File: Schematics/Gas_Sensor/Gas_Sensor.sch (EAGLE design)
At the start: 7 parts, among them J1 RJ45

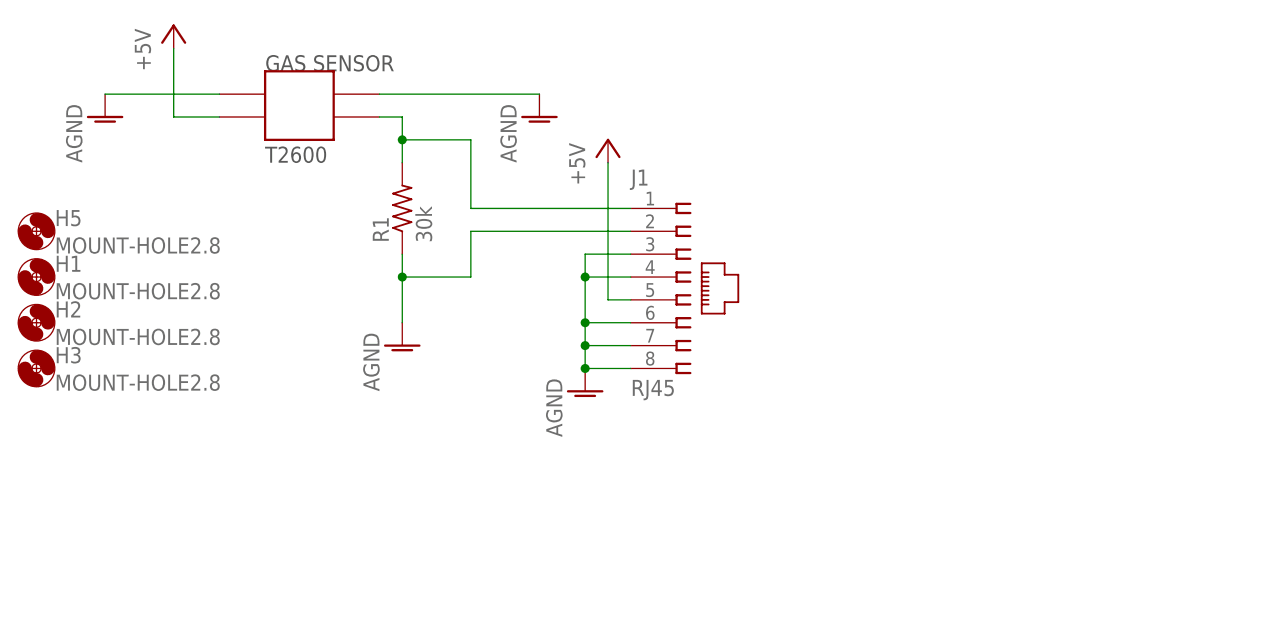
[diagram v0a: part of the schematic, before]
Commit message: Updated Sensor Module PCBs
Switched Ethernet I/O. Rerouted PCB
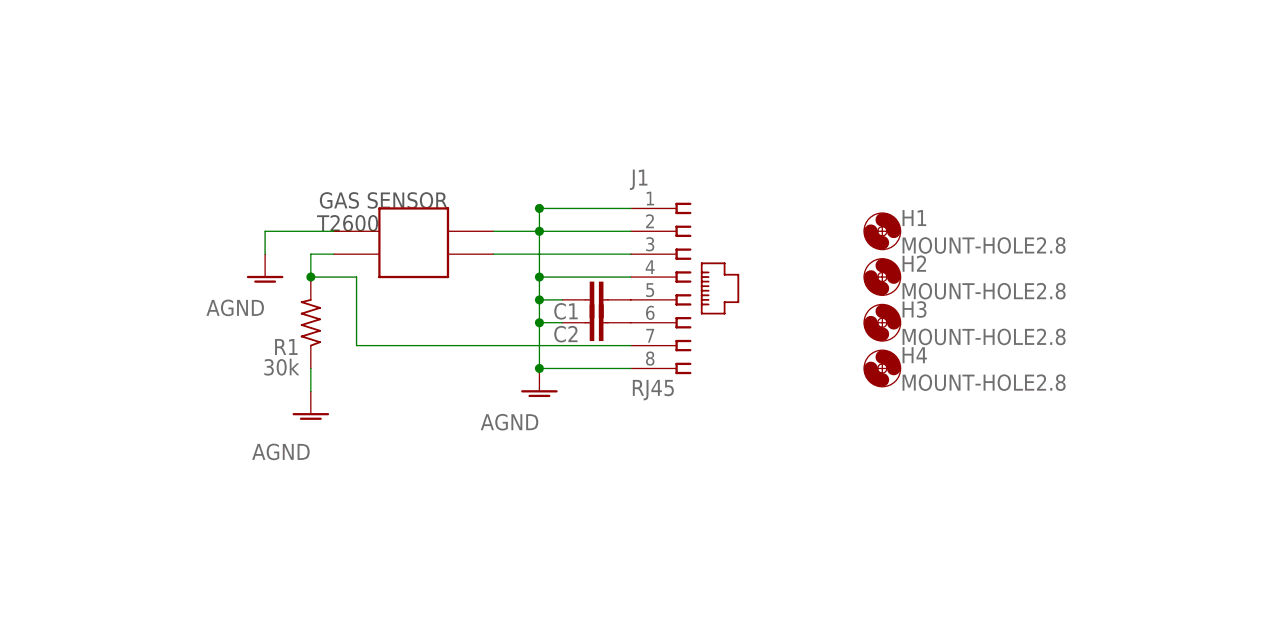
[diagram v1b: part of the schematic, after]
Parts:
- removed H5: MOUNT-HOLE2.8, holes:MOUNT-HOLE2.8
- added C1, C2: (no value), rcl:C-EUC0603K
- added H4: MOUNT-HOLE2.8, holes:MOUNT-HOLE2.8
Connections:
- removed net +5V: J1.5, U$1.P$3
- new net N$24: C2.1, J1.6
- new net N$25: C1.1, J1.5
- new net N$26: J1.3, U$1.P$3
- net AGND: now also C1.2, C2.2, J1.1; no longer J1.3, J1.6, J1.7
- net N$2: now also J1.7; no longer J1.1
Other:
- moved on the sheet: H1, H2, H3, R1

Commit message: Began PCB Verify. Slight Modifications to Gas Sensor Module during verify.
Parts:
- renumbered U$1 to X1
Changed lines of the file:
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@@
 <grid distance="0.1" unitdist="inch" unit="inch" style="lines" multiple="1" display="no" altdistance="0.01" altunitdist="inch" altunit="inch"/>
 <layers>
-<layer number="1" name="Top" color="4" fill="1" visible="no" active="no"/>
-<layer number="16" name="Bottom" color="1" fill="1" visible="no" active="no"/>
-<layer number="17" name="Pads" color="2" fill="1" visible="no" active="no"/>
-<layer number="18" name="Vias" color="2" fill="1" visible="no" active="no"/>
-<layer number="19" name="Unrouted" color="6" fill="1" visible="no" active="no"/>
-<layer number="20" name="Dimension" color="15" fill="1" visible="no" active="no"/>
-<layer number="21" name="tPlace" color="7" fill="1" visible="no" active="no"/>
-<layer number="22" name="bPlace" color="7" fill="1" visible="no" active="no"/>
-<layer number="23" name="tOrigins" color="15" fill="1" visible="no" active="no"/>
-<layer number="24" name="bOrigins" color="15" fill="1" visible="no" active="no"/>
-<layer number="25" name="tNames" color="7" fill="1" visible="no" active="no"/>
-<layer number="26" name="bNames" color="7" fill="1" visible="no" active="no"/>
-<layer number="27" name="tValues" color="7" fill="1" visible="no" active="no"/>
-<layer number="28" name="bValues" color="7" fill="1" visible="no" active="no"/>
+<layer number="1" name="Top" color="4" fill="1" visible="yes" active="no"/>
+<layer number="16" name="Bottom" color="1" fill="1" visible="yes" active="no"/>
+<layer number="17" name="Pads" color="2" fill="1" visible="yes" active="no"/>
+<layer number="18" name="Vias" color="2" fill="1" visible="yes" active="no"/>
+<layer number="19" name="Unrouted" color="6" fill="1" visible="yes" active="no"/>
+<layer number="20" name="Dimension" color="15" fill="1" visible="yes" active="no"/>
+<layer number="21" name="tPlace" color="7" fill="1" visible="yes" active="no"/>
+<layer number="22" name="bPlace" color="7" fill="1" visible="yes" active="no"/>
+<layer number="23" name="tOrigins" color="15" fill="1" visible="yes" active="no"/>
+<layer number="24" name="bOrigins" color="15" fill="1" visible="yes" active="no"/>
+<layer number="25" name="tNames" color="7" fill="1" visible="yes" active="no"/>
+<layer number="26" name="bNames" color="7" fill="1" visible="yes" active="no"/>
+<layer number="27" name="tValues" color="7" fill="1" visible="yes" active="no"/>
+<layer number="28" name="bValues" color="7" fill="1" visible="yes" active="no"/>
 <layer number="29" name="tStop" color="7" fill="3" visible="no" active="no"/>
 <layer number="30" name="bStop" color="7" fill="6" visible="no" active="no"/>
@@
 <layer number="35" name="tGlue" color="7" fill="4" visible="no" active="no"/>
 <layer number="36" name="bGlue" color="7" fill="5" visible="no" active="no"/>
-<layer number="37" name="tTest" color="7" fill="1" visible="no" active="no"/>
-<layer number="38" name="bTest" color="7" fill="1" visible="no" active="no"/>
+<layer number="37" name="tTest" color="7" fill="1" visible="yes" active="no"/>
+<layer number="38" name="bTest" color="7" fill="1" visible="yes" active="no"/>
 <layer number="39" name="tKeepout" color="4" fill="11" visible="no" active="no"/>
 <layer number="40" name="bKeepout" color="1" fill="11" visible="no" active="no"/>
@@
 <layer number="44" name="Drills" color="7" fill="1" visible="no" active="no"/>
 <layer number="45" name="Holes" color="7" fill="1" visible="no" active="no"/>
-<layer number="46" name="Milling" color="3" fill="1" visible="no" active="no"/>
-<layer number="47" name="Measures" color="7" fill="1" visible="no" active="no"/>
-<layer number="48" name="Document" color="7" fill="1" visible="no" active="no"/>
-<layer number="49" name="Reference" color="7" fill="1" visible="no" active="no"/>
-<layer number="51" name="tDocu" color="7" fill="1" visible="no" active="no"/>
-<layer number="52" name="bDocu" color="7" fill="1" visible="no" active="no"/>
+<layer number="46" name="Milling" color="3" fill="1" visible="yes" active="no"/>
+<layer number="47" name="Measures" color="7" fill="1" visible="yes" active="no"/>
+<layer number="48" name="Document" color="7" fill="1" visible="yes" active="no"/>
+<layer number="49" name="Reference" color="7" fill="1" visible="yes" active="no"/>
+<layer number="51" name="tDocu" color="7" fill="1" visible="yes" active="no"/>
+<layer number="52" name="bDocu" color="7" fill="1" visible="yes" active="no"/>
 <layer number="91" name="Nets" color="2" fill="1" visible="yes" active="yes"/>
 <layer number="92" name="Busses" color="1" fill="1" visible="yes" active="yes"/>
@@
 </classes>
 <parts>
-<part name="U$1" library="figaro" deviceset="GAS_SENSOR" device=""/>
+<part name="X1" library="figaro" deviceset="GAS_SENSOR" device=""/>
 <part name="AGND1" library="supply1" deviceset="AGND" device=""/>
 <part name="R1" library="rcl" deviceset="R-US_" device="R1206" value="30k"/>
@@
 </plain>
 <instances>
-<instance part="U$1" gate="GAS" x="71.12" y="45.72" rot="MR0"/>
+<instance part="X1" gate="GAS" x="71.12" y="45.72" rot="MR0"/>
 <instance part="AGND1" gate="VR1" x="53.34" y="43.18" smashed="yes">
 <attribute name="VALUE" x="53.34" y="40.64" size="1.778" layer="96" rot="R180"/>
@@
 <wire x1="93.98" y1="43.18" x2="83.82" y2="43.18" width="0.1524" layer="91"/>
 <junction x="83.82" y="43.18"/>
-<pinref part="U$1" gate="GAS" pin="P$4"/>
+<pinref part="X1" gate="GAS" pin="P$4"/>
 <wire x1="78.74" y1="48.26" x2="83.82" y2="48.26" width="0.1524" layer="91"/>
 <wire x1="83.82" y1="48.26" x2="83.82" y2="50.8" width="0.1524" layer="91"/>
@@
 </segment>
 <segment>
-<pinref part="U$1" gate="GAS" pin="P$1"/>
+<pinref part="X1" gate="GAS" pin="P$1"/>
 <wire x1="60.96" y1="48.26" x2="53.34" y2="48.26" width="0.1524" layer="91"/>
 <pinref part="AGND1" gate="VR1" pin="AGND"/>
@@
 <segment>
 <pinref part="R1" gate="G$1" pin="2"/>
-<pinref part="U$1" gate="GAS" pin="P$2"/>
+<pinref part="X1" gate="GAS" pin="P$2"/>
 <wire x1="58.42" y1="43.18" x2="58.42" y2="45.72" width="0.1524" layer="91"/>
 <wire x1="58.42" y1="45.72" x2="60.96" y2="45.72" width="0.1524" layer="91"/>
@@
 <pinref part="J1" gate="G$1" pin="3"/>
 <wire x1="93.98" y1="45.72" x2="78.74" y2="45.72" width="0.1524" layer="91"/>
-<pinref part="U$1" gate="GAS" pin="P$3"/>
+<pinref part="X1" gate="GAS" pin="P$3"/>
 </segment>
 </net>

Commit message: Layout for final inspection
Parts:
- C1, C2: value (none) -> 0.1uF
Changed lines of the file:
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@@
 <?xml version="1.0" encoding="utf-8"?>
 <!DOCTYPE eagle SYSTEM "eagle.dtd">
-<eagle version="6.3">
+<eagle version="6.4">
 <drawing>
 <settings>
@@
 <grid distance="0.1" unitdist="inch" unit="inch" style="lines" multiple="1" display="no" altdistance="0.01" altunitdist="inch" altunit="inch"/>
 <layers>
-<layer number="1" name="Top" color="4" fill="1" visible="yes" active="no"/>
-<layer number="16" name="Bottom" color="1" fill="1" visible="yes" active="no"/>
-<layer number="17" name="Pads" color="2" fill="1" visible="yes" active="no"/>
-<layer number="18" name="Vias" color="2" fill="1" visible="yes" active="no"/>
-<layer number="19" name="Unrouted" color="6" fill="1" visible="yes" active="no"/>
-<layer number="20" name="Dimension" color="15" fill="1" visible="yes" active="no"/>
-<layer number="21" name="tPlace" color="7" fill="1" visible="yes" active="no"/>
-<layer number="22" name="bPlace" color="7" fill="1" visible="yes" active="no"/>
-<layer number="23" name="tOrigins" color="15" fill="1" visible="yes" active="no"/>
-<layer number="24" name="bOrigins" color="15" fill="1" visible="yes" active="no"/>
-<layer number="25" name="tNames" color="7" fill="1" visible="yes" active="no"/>
-<layer number="26" name="bNames" color="7" fill="1" visible="yes" active="no"/>
-<layer number="27" name="tValues" color="7" fill="1" visible="yes" active="no"/>
-<layer number="28" name="bValues" color="7" fill="1" visible="yes" active="no"/>
+<layer number="1" name="Top" color="4" fill="1" visible="no" active="no"/>
+<layer number="16" name="Bottom" color="1" fill="1" visible="no" active="no"/>
+<layer number="17" name="Pads" color="2" fill="1" visible="no" active="no"/>
+<layer number="18" name="Vias" color="2" fill="1" visible="no" active="no"/>
+<layer number="19" name="Unrouted" color="6" fill="1" visible="no" active="no"/>
+<layer number="20" name="Dimension" color="15" fill="1" visible="no" active="no"/>
+<layer number="21" name="tPlace" color="7" fill="1" visible="no" active="no"/>
+<layer number="22" name="bPlace" color="7" fill="1" visible="no" active="no"/>
+<layer number="23" name="tOrigins" color="15" fill="1" visible="no" active="no"/>
+<layer number="24" name="bOrigins" color="15" fill="1" visible="no" active="no"/>
+<layer number="25" name="tNames" color="7" fill="1" visible="no" active="no"/>
+<layer number="26" name="bNames" color="7" fill="1" visible="no" active="no"/>
+<layer number="27" name="tValues" color="7" fill="1" visible="no" active="no"/>
+<layer number="28" name="bValues" color="7" fill="1" visible="no" active="no"/>
 <layer number="29" name="tStop" color="7" fill="3" visible="no" active="no"/>
 <layer number="30" name="bStop" color="7" fill="6" visible="no" active="no"/>
@@
 <layer number="35" name="tGlue" color="7" fill="4" visible="no" active="no"/>
 <layer number="36" name="bGlue" color="7" fill="5" visible="no" active="no"/>
-<layer number="37" name="tTest" color="7" fill="1" visible="yes" active="no"/>
-<layer number="38" name="bTest" color="7" fill="1" visible="yes" active="no"/>
+<layer number="37" name="tTest" color="7" fill="1" visible="no" active="no"/>
+<layer number="38" name="bTest" color="7" fill="1" visible="no" active="no"/>
 <layer number="39" name="tKeepout" color="4" fill="11" visible="no" active="no"/>
 <layer number="40" name="bKeepout" color="1" fill="11" visible="no" active="no"/>
@@
 <layer number="44" name="Drills" color="7" fill="1" visible="no" active="no"/>
 <layer number="45" name="Holes" color="7" fill="1" visible="no" active="no"/>
-<layer number="46" name="Milling" color="3" fill="1" visible="yes" active="no"/>
-<layer number="47" name="Measures" color="7" fill="1" visible="yes" active="no"/>
-<layer number="48" name="Document" color="7" fill="1" visible="yes" active="no"/>
-<layer number="49" name="Reference" color="7" fill="1" visible="yes" active="no"/>
-<layer number="51" name="tDocu" color="7" fill="1" visible="yes" active="no"/>
-<layer number="52" name="bDocu" color="7" fill="1" visible="yes" active="no"/>
+<layer number="46" name="Milling" color="3" fill="1" visible="no" active="no"/>
+<layer number="47" name="Measures" color="7" fill="1" visible="no" active="no"/>
+<layer number="48" name="Document" color="7" fill="1" visible="no" active="no"/>
+<layer number="49" name="Reference" color="7" fill="1" visible="no" active="no"/>
+<layer number="51" name="tDocu" color="7" fill="1" visible="no" active="no"/>
+<layer number="52" name="bDocu" color="7" fill="1" visible="no" active="no"/>
 <layer number="91" name="Nets" color="2" fill="1" visible="yes" active="yes"/>
 <layer number="92" name="Busses" color="1" fill="1" visible="yes" active="yes"/>
@@
 <part name="H2" library="holes" deviceset="MOUNT-HOLE" device="2.8"/>
 <part name="H3" library="holes" deviceset="MOUNT-HOLE" device="2.8"/>
-<part name="C1" library="rcl" deviceset="C-EU" device="C0603K"/>
-<part name="C2" library="rcl" deviceset="C-EU" device="C0603K"/>
+<part name="C1" library="rcl" deviceset="C-EU" device="C0603K" value="0.1uF"/>
+<part name="C2" library="rcl" deviceset="C-EU" device="C0603K" value="0.1uF"/>
 </parts>
 <sheets>

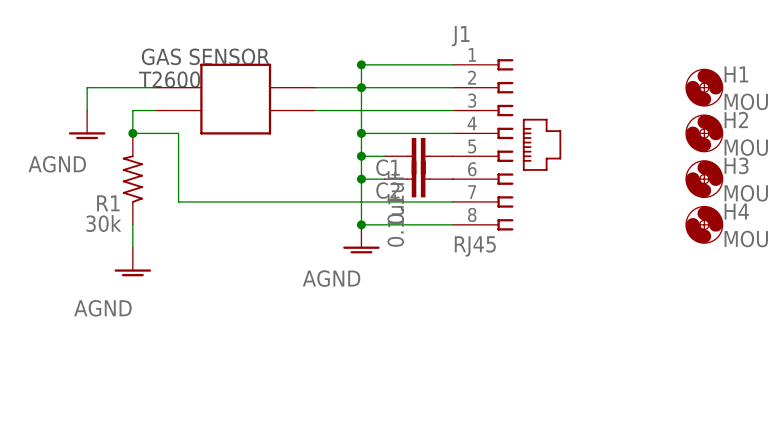
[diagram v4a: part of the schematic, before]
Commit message: Cleaned up stuff
Made Schematics easier to read
Split Supplies in BOM and made names match references
Renamed parts on sensor
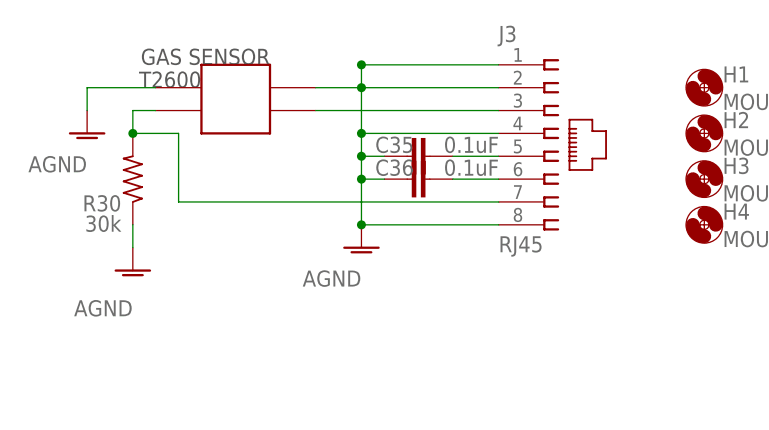
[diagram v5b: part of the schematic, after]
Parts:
- removed J1: RJ45, con-amp:555167-1
- added J3: RJ45, con-amp:555167-1
- renumbered C1 to C35, C2 to C36, R1 to R30
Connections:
- net AGND: now also J3.1, J3.2, J3.4, J3.8; no longer J1.1, J1.2, J1.4, J1.8
- net N$2: now also J3.7; no longer J1.7
- net N$24: now also J3.6; no longer J1.6
- net N$25: now also J3.5; no longer J1.5
- net N$26: now also J3.3; no longer J1.3

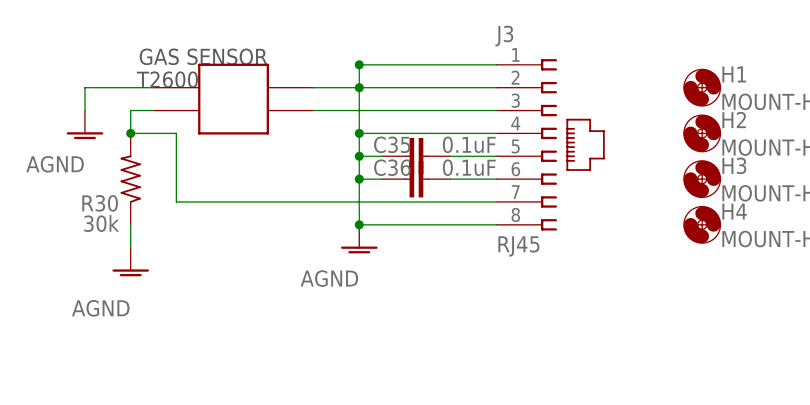
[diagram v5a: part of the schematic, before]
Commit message: Boo Boo fix on Gas Sensor
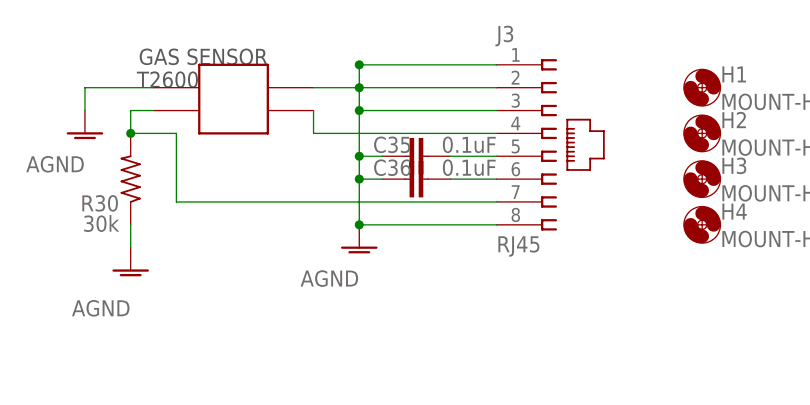
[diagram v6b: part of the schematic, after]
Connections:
- removed net N$26: J3.3, X1.P$3
- new net N$1: J3.4, X1.P$3
- net AGND: now also J3.3; no longer J3.4
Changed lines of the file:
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@@
 <pinref part="AGND4" gate="VR1" pin="AGND"/>
 <pinref part="J3" gate="G$1" pin="2"/>
-<wire x1="83.82" y1="48.26" x2="83.82" y2="43.18" width="0.1524" layer="91"/>
-<wire x1="83.82" y1="43.18" x2="83.82" y2="40.64" width="0.1524" layer="91"/>
+<wire x1="83.82" y1="48.26" x2="83.82" y2="45.72" width="0.1524" layer="91"/>
+<wire x1="83.82" y1="45.72" x2="83.82" y2="40.64" width="0.1524" layer="91"/>
 <wire x1="83.82" y1="40.64" x2="83.82" y2="38.1" width="0.1524" layer="91"/>
 <wire x1="83.82" y1="38.1" x2="83.82" y2="33.02" width="0.1524" layer="91"/>
@@
 <wire x1="86.36" y1="38.1" x2="83.82" y2="38.1" width="0.1524" layer="91"/>
 <junction x="83.82" y="38.1"/>
-<pinref part="J3" gate="G$1" pin="4"/>
-<wire x1="99.06" y1="43.18" x2="83.82" y2="43.18" width="0.1524" layer="91"/>
-<junction x="83.82" y="43.18"/>
 <pinref part="X1" gate="GAS" pin="P$4"/>
 <wire x1="78.74" y1="48.26" x2="83.82" y2="48.26" width="0.1524" layer="91"/>
@@
 <wire x1="83.82" y1="33.02" x2="99.06" y2="33.02" width="0.1524" layer="91"/>
 <junction x="83.82" y="33.02"/>
+<pinref part="J3" gate="G$1" pin="3"/>
+<wire x1="99.06" y1="45.72" x2="83.82" y2="45.72" width="0.1524" layer="91"/>
+<junction x="83.82" y="45.72"/>
 </segment>
 <segment>
@@
 </segment>
 </net>
-<net name="N$26" class="0">
+<net name="N$1" class="0">
 <segment>
-<pinref part="J3" gate="G$1" pin="3"/>
-<wire x1="99.06" y1="45.72" x2="78.74" y2="45.72" width="0.1524" layer="91"/>
+<pinref part="J3" gate="G$1" pin="4"/>
 <pinref part="X1" gate="GAS" pin="P$3"/>
+<wire x1="99.06" y1="43.18" x2="78.74" y2="43.18" width="0.1524" layer="91"/>
+<wire x1="78.74" y1="43.18" x2="78.74" y2="45.72" width="0.1524" layer="91"/>
 </segment>
 </net>
